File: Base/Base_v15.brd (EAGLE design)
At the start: 100 x 54.5 mm, 17 parts, among them IC1 74HC595, IC2 74HC595, IC3 K155ID, IC4 K155ID, IC5 K155ID, IC6 K155ID, J1 694106301002, J2 694106301002, K1 ZNS5106, Q1 PNP

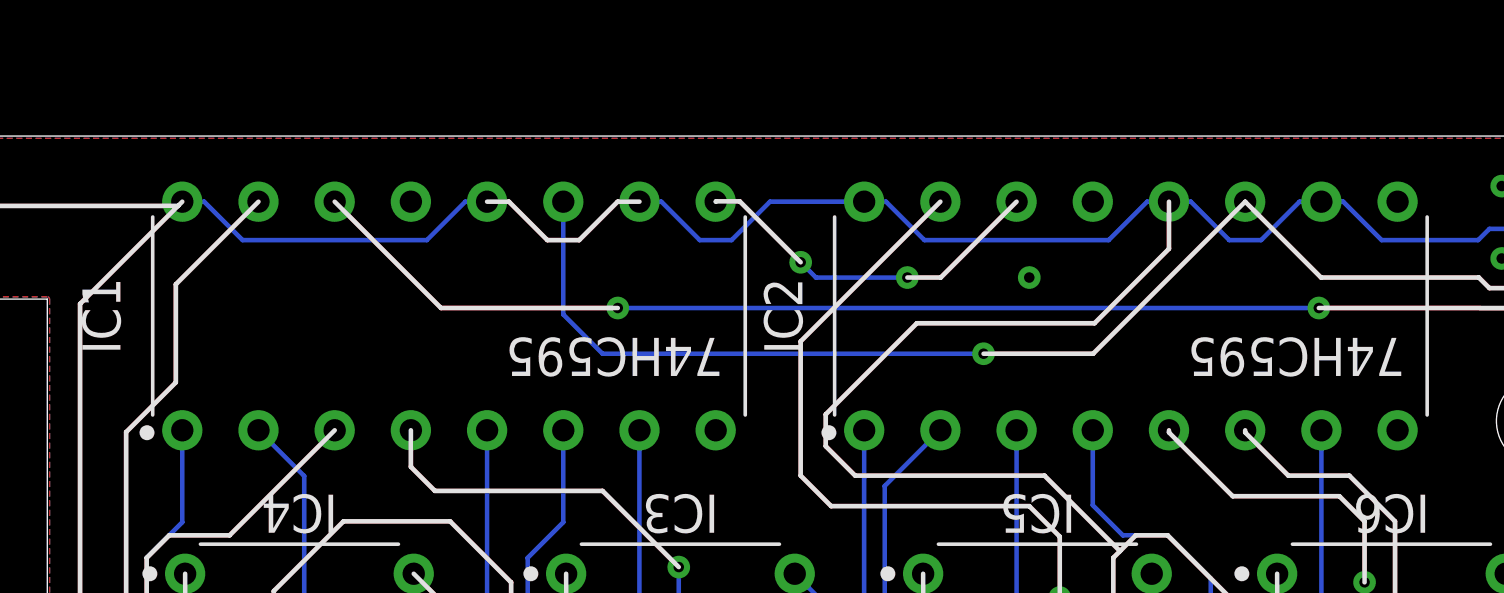
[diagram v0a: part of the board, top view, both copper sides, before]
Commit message: Fixed shift register clock lines
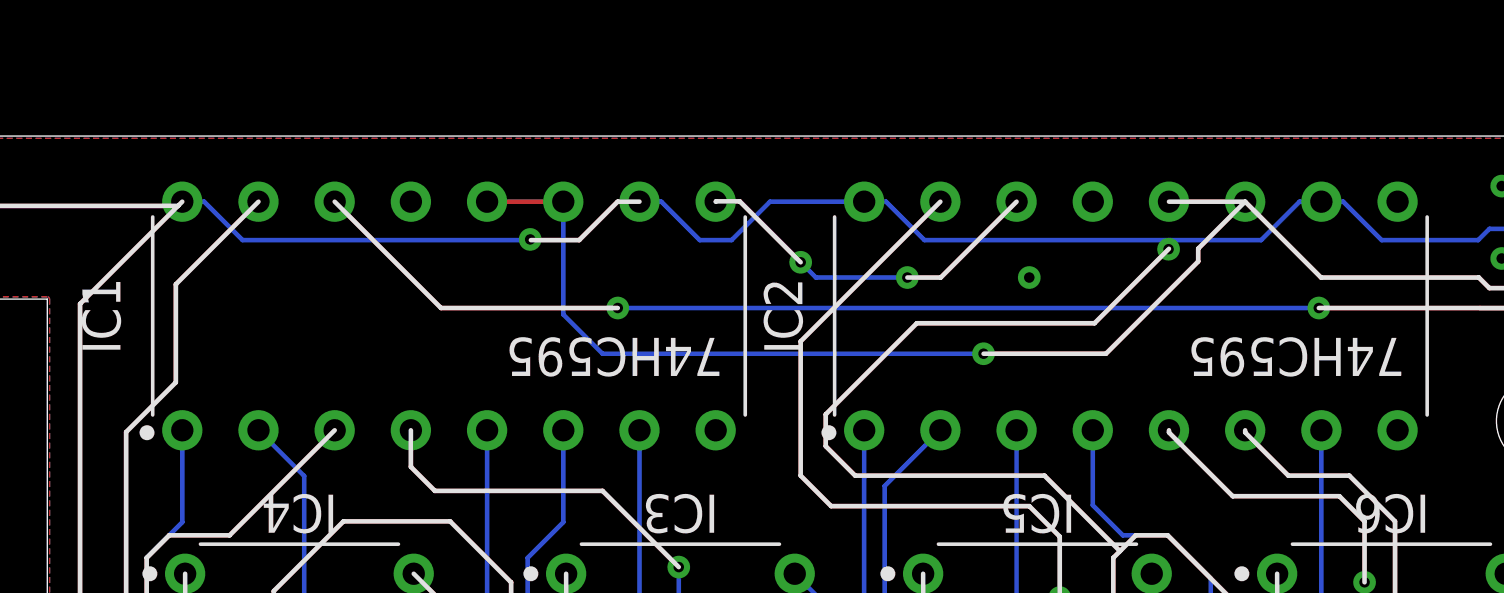
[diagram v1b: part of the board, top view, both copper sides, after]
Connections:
- net N$58: now also IC1.12, IC2.12
- net VCC: no longer IC1.12, IC2.12
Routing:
- net N$58: track 52.6 -> 57.9 mm
- net VCC: track 294.5 -> 291.1 mm, vias 2 -> 4
